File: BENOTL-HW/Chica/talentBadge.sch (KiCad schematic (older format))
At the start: 63 parts, among them P1 USB_A, P2 OLED, P3 Batt, P4 PS, P5 sd_card_spi, Q1 MMBT3904, Q2 MMBT3904, Q3 IR phototransistor, SW1 B1, SW2 B2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

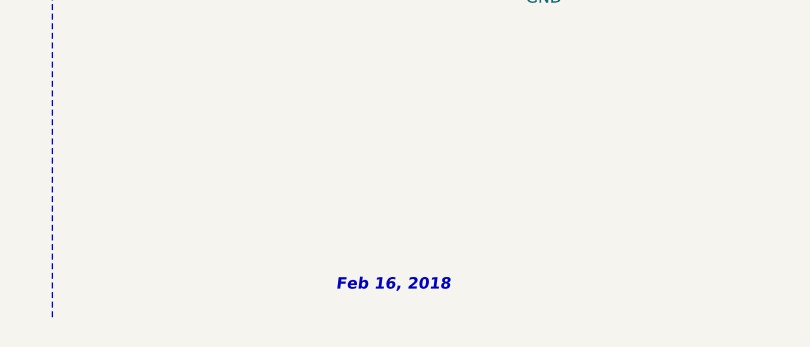
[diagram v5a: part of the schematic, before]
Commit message: Vinculado footprint ESP-WROOM-02
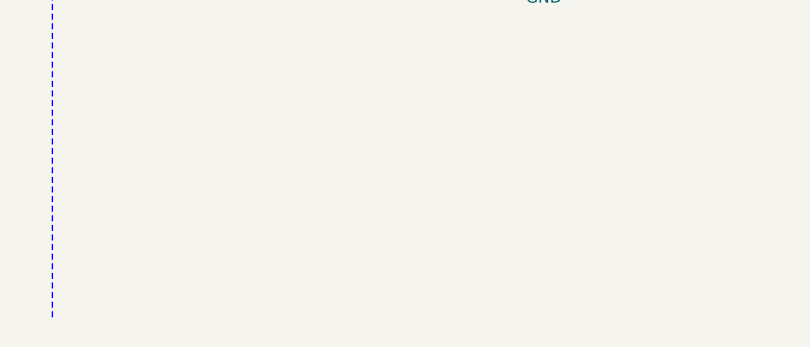
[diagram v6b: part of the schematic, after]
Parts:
- U1: footprint (none) -> talentBadge:ESP-13-WROOM-02
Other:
- note removed: "Feb 16, 2018\n"
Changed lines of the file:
@@
 $EndComp
 $Comp
-L GND #PWR8
+L GND #PWR01
 U 1 1 5A821F87
 P 2900 7450
-F 0 "#PWR8" H 2900 7200 50  0001 C CNN
+F 0 "#PWR01" H 2900 7200 50  0001 C CNN
 F 1 "GND" H 2900 7300 50  0000 C CNN
 F 2 "" H 2900 7450 50  0000 C CNN
@@
 $EndComp
 $Comp
-L GND #PWR6
+L GND #PWR02
 U 1 1 5A8731F6
 P 2550 3100
-F 0 "#PWR6" H 2550 2850 50  0001 C CNN
+F 0 "#PWR02" H 2550 2850 50  0001 C CNN
 F 1 "GND" H 2550 2950 50  0000 C CNN
 F 2 "" H 2550 3100 50  0000 C CNN
@@
 np1
 $Comp
-L GND #PWR11
+L GND #PWR03
 U 1 1 5A87C4F2
 P 4350 3100
-F 0 "#PWR11" H 4350 2850 50  0001 C CNN
+F 0 "#PWR03" H 4350 2850 50  0001 C CNN
 F 1 "GND" H 4350 2950 50  0000 C CNN
 F 2 "" H 4350 3100 50  0000 C CNN
@@
 np2
 $Comp
-L GND #PWR16
+L GND #PWR04
 U 1 1 5A87E79A
 P 6150 3100
-F 0 "#PWR16" H 6150 2850 50  0001 C CNN
+F 0 "#PWR04" H 6150 2850 50  0001 C CNN
 F 1 "GND" H 6150 2950 50  0000 C CNN
 F 2 "" H 6150 3100 50  0000 C CNN
@@
 $EndComp
 $Comp
-L GND #PWR3
+L GND #PWR05
 U 1 1 5A884E23
 P 1700 6900
-F 0 "#PWR3" H 1700 6650 50  0001 C CNN
+F 0 "#PWR05" H 1700 6650 50  0001 C CNN
 F 1 "GND" H 1700 6750 50  0000 C CNN
 F 2 "" H 1700 6900 50  0000 C CNN
@@
 $EndComp
 $Comp
-L +3.3V #PWR5
+L +3.3V #PWR06
 U 1 1 5A8855B6
 P 2250 6200
-F 0 "#PWR5" H 2250 6050 50  0001 C CNN
+F 0 "#PWR06" H 2250 6050 50  0001 C CNN
 F 1 "+3.3V" H 2250 6340 50  0000 C CNN
 F 2 "" H 2250 6200 50  0000 C CNN
@@
 np
 $Comp
-L +3.3V #PWR1
+L +3.3V #PWR07
 U 1 1 5A888CD9
 P 1000 950
-F 0 "#PWR1" H 1000 800 50  0001 C CNN
+F 0 "#PWR07" H 1000 800 50  0001 C CNN
 F 1 "+3.3V" H 1000 1090 50  0000 C CNN
 F 2 "" H 1000 950 50  0000 C CNN
@@
 $EndComp
 $Comp
-L +3.3V #PWR7
+L +3.3V #PWR08
 U 1 1 5A888D9D
 P 2850 950
-F 0 "#PWR7" H 2850 800 50  0001 C CNN
+F 0 "#PWR08" H 2850 800 50  0001 C CNN
 F 1 "+3.3V" H 2850 1090 50  0000 C CNN
 F 2 "" H 2850 950 50  0000 C CNN
@@
 $EndComp
 $Comp
-L +3.3V #PWR13
+L +3.3V #PWR09
 U 1 1 5A88959B
 P 4550 950
-F 0 "#PWR13" H 4550 800 50  0001 C CNN
+F 0 "#PWR09" H 4550 800 50  0001 C CNN
 F 1 "+3.3V" H 4550 1090 50  0000 C CNN
 F 2 "" H 4550 950 50  0000 C CNN
@@
 $EndComp
 $Comp
-L GND #PWR21
+L GND #PWR010
 U 1 1 5A889D35
 P 8100 2640
-F 0 "#PWR21" H 8100 2390 50  0001 C CNN
+F 0 "#PWR010" H 8100 2390 50  0001 C CNN
 F 1 "GND" H 8100 2490 50  0000 C CNN
 F 2 "" H 8100 2640 50  0000 C CNN
@@
 MISO
 $Comp
-L GND #PWR2
+L GND #PWR011
 U 1 1 5A89D556
 P 1400 4300
-F 0 "#PWR2" H 1400 4050 50  0001 C CNN
+F 0 "#PWR011" H 1400 4050 50  0001 C CNN
 F 1 "GND" H 1400 4150 50  0000 C CNN
 F 2 "" H 1400 4300 50  0000 C CNN
@@
 $EndComp
 $Comp
-L +3.3V #PWR4
+L +3.3V #PWR012
 U 1 1 5A89DD80
 P 1900 3850
-F 0 "#PWR4" H 1900 3700 50  0001 C CNN
+F 0 "#PWR012" H 1900 3700 50  0001 C CNN
 F 1 "+3.3V" H 1900 3990 50  0000 C CNN
 F 2 "" H 1900 3850 50  0000 C CNN
@@
 $EndComp
 $Comp
-L GND #PWR9
+L GND #PWR013
 U 1 1 5A8A120C
 P 3050 5200
-F 0 "#PWR9" H 3050 4950 50  0001 C CNN
+F 0 "#PWR013" H 3050 4950 50  0001 C CNN
 F 1 "GND" H 3050 5050 50  0000 C CNN
 F 2 "" H 3050 5200 50  0000 C CNN
@@
 	1    0    0    -1
 $EndComp
-Text Notes 8140 7640 0    50   Italic 10
-Feb 16, 2018\n
-$Comp
-L +3.3V #PWR23
+$Comp
+L +3.3V #PWR014
 U 1 1 5A8ACE92
 P 8750 4150
-F 0 "#PWR23" H 8750 4000 50  0001 C CNN
+F 0 "#PWR014" H 8750 4000 50  0001 C CNN
 F 1 "+3.3V" H 8750 4290 50  0000 C CNN
 F 2 "" H 8750 4150 50  0000 C CNN
@@
 $EndComp
 $Comp
-L GND #PWR22
+L GND #PWR015
 U 1 1 5A8B6B0C
 P 8600 4600
-F 0 "#PWR22" H 8600 4350 50  0001 C CNN
+F 0 "#PWR015" H 8600 4350 50  0001 C CNN
 F 1 "GND" H 8450 4550 50  0000 C CNN
 F 2 "" H 8600 4600 50  0000 C CNN
@@
 $EndComp
 $Comp
-L GND #PWR24
+L GND #PWR016
 U 1 1 5A8BA4F2
 P 9050 6200
-F 0 "#PWR24" H 9050 5950 50  0001 C CNN
+F 0 "#PWR016" H 9050 5950 50  0001 C CNN
 F 1 "GND" H 9050 6050 50  0000 C CNN
 F 2 "" H 9050 6200 50  0000 C CNN
@@
 $EndComp
 $Comp
-L +3.3V #PWR10
+L +3.3V #PWR017
 U 1 1 5A8CF103
 P 3700 6000
-F 0 "#PWR10" H 3700 5850 50  0001 C CNN
+F 0 "#PWR017" H 3700 5850 50  0001 C CNN
 F 1 "+3.3V" H 3700 6140 50  0000 C CNN
 F 2 "" H 3700 6000 50  0000 C CNN
@@
 $EndComp
 $Comp
-L +3.3V #PWR12
+L +3.3V #PWR018
 U 1 1 5A8CF265
 P 4535 4300
-F 0 "#PWR12" H 4535 4150 50  0001 C CNN
+F 0 "#PWR018" H 4535 4150 50  0001 C CNN
 F 1 "+3.3V" H 4535 4440 50  0000 C CNN
 F 2 "" H 4535 4300 50  0000 C CNN
@@
 $EndComp
 $Comp
-L GND #PWR14
+L GND #PWR019
 U 1 1 5A8CFC33
 P 4650 4900
-F 0 "#PWR14" H 4650 4650 50  0001 C CNN
+F 0 "#PWR019" H 4650 4650 50  0001 C CNN
 F 1 "GND" H 4650 4750 50  0000 C CNN
 F 2 "" H 4650 4900 50  0000 C CNN
@@
 IRL
 $Comp
-L GND #PWR18
+L GND #PWR020
 U 1 1 5A914774
 P 6200 5150
-F 0 "#PWR18" H 6200 4900 50  0001 C CNN
+F 0 "#PWR020" H 6200 4900 50  0001 C CNN
 F 1 "GND" H 6200 5000 50  0000 C CNN
 F 2 "" H 6200 5150 50  0000 C CNN
@@
 $EndComp
 $Comp
-L +3.3V #PWR17
+L +3.3V #PWR021
 U 1 1 5A916FB2
 P 6200 3850
-F 0 "#PWR17" H 6200 3700 50  0001 C CNN
+F 0 "#PWR021" H 6200 3700 50  0001 C CNN
 F 1 "+3.3V" H 6200 3990 50  0000 C CNN
 F 2 "" H 6200 3850 50  0000 C CNN
@@
 $EndComp
 $Comp
-L +3.3V #PWR19
+L +3.3V #PWR022
 U 1 1 5A8CED38
 P 7775 1585
-F 0 "#PWR19" H 7775 1435 50  0001 C CNN
+F 0 "#PWR022" H 7775 1435 50  0001 C CNN
 F 1 "+3.3V" H 7775 1725 50  0000 C CNN
 F 2 "" H 7775 1585 50  0000 C CNN
@@
 NoConn ~ 10550 4800
 $Comp
-L GND #PWR15
+L GND #PWR023
 U 1 1 5A9146B5
 P 5700 5150
-F 0 "#PWR15" H 5700 4900 50  0001 C CNN
+F 0 "#PWR023" H 5700 4900 50  0001 C CNN
 F 1 "GND" H 5700 5000 50  0000 C CNN
 F 2 "" H 5700 5150 50  0000 C CNN
@@
 F 0 "U1" H 9315 1940 50  0000 C CNN
 F 1 "ESP-13-WROOM-02" H 9315 2490 50  0000 C CNN
-F 2 "" H 9215 2040 50  0001 C CNN
+F 2 "talentBadge:ESP-13-WROOM-02" H 9215 2040 50  0001 C CNN
 F 3 "" H 9215 2040 50  0001 C CNN
 	1    9315 2040
@@
 Connection ~ 8030 1475
 $Comp
-L +3.3V #PWR20
+L +3.3V #PWR024
 U 1 1 5AA16781
 P 8025 1415
-F 0 "#PWR20" H 8025 1265 50  0001 C CNN
+F 0 "#PWR024" H 8025 1265 50  0001 C CNN
 F 1 "+3.3V" H 8025 1555 50  0000 C CNN
 F 2 "" H 8025 1415 50  0000 C CNN
@@
 $EndComp
 $Comp
-L GND #PWR25
+L GND #PWR025
 U 1 1 5AA16E5F
 P 10830 2575
-F 0 "#PWR25" H 10830 2325 50  0001 C CNN
+F 0 "#PWR025" H 10830 2325 50  0001 C CNN
 F 1 "GND" H 10830 2425 50  0000 C CNN
 F 2 "" H 10830 2575 50  0000 C CNN
@@
 	9315 2940 9315 3060
 $Comp
-L GND #PWR?
+L GND #PWR026
 U 1 1 5AA1CD61
 P 9315 3060
-F 0 "#PWR?" H 9315 2810 50  0001 C CNN
+F 0 "#PWR026" H 9315 2810 50  0001 C CNN
 F 1 "GND" H 9315 2910 50  0000 C CNN
 F 2 "" H 9315 3060 50  0000 C CNN

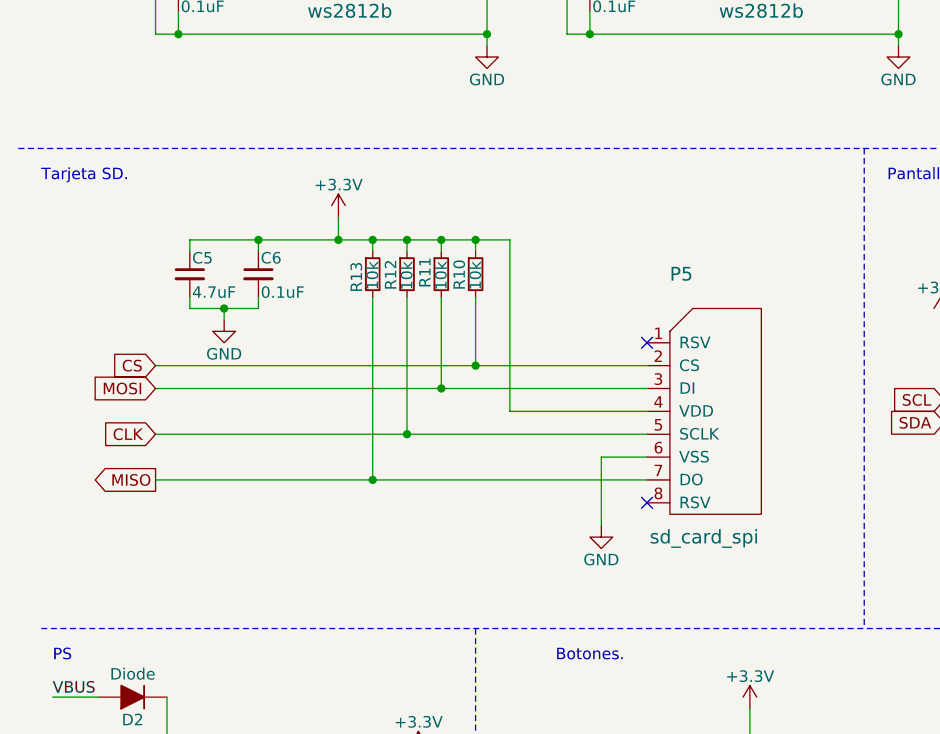
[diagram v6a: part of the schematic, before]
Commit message: Removido diagrama SD
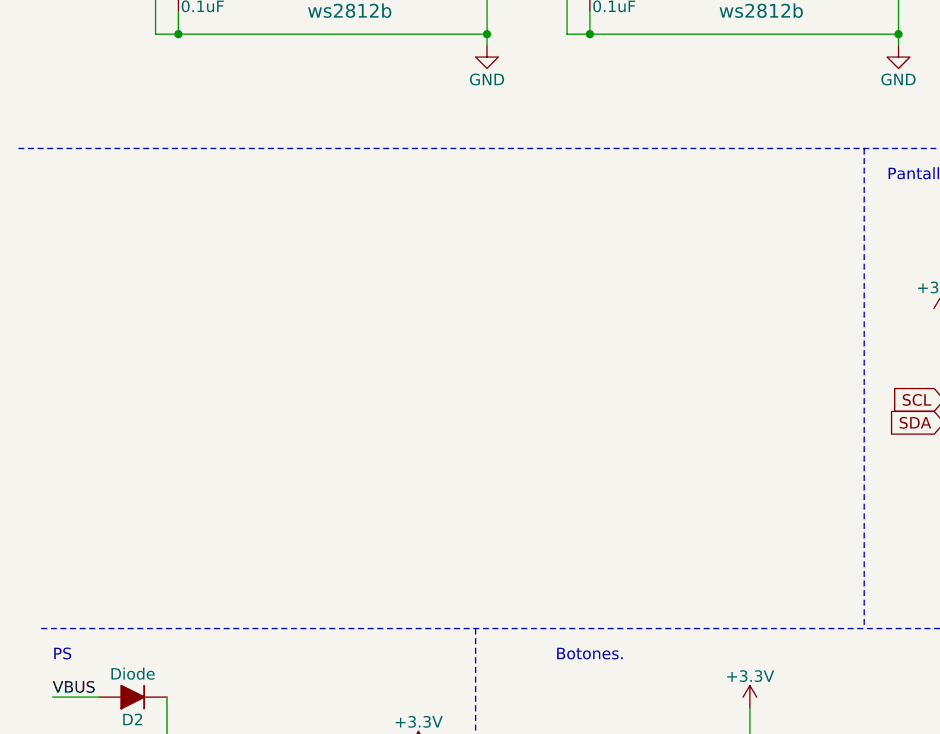
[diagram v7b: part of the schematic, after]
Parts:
- removed C5: 4.7uF, Capacitors_SMD:C_0805_HandSoldering, symbol C_Small
- removed C6: 0.1uF, Capacitors_SMD:C_0805_HandSoldering, symbol C_Small
- removed P5: sd_card_spi, talentBadge:MOLEX_0475710001, symbol sd_card_spi
- removed R10, R11, R12, R13: 10k, Resistors_SMD:R_0805_HandSoldering, symbol R_Small
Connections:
- no-connect marks 20 -> 18
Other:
- note removed: "Tarjeta SD."
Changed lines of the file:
@@
 Title "The badge of the Lands"
 Date "2018-03-07"
-Rev "0.3"
+Rev "0.4"
 Comp "Unofficial Badge of Talent Land 2018"
 Comment1 "Andres Sabas"
@@
 Text GLabel 10485 2535 2    50   Input ~ 0
 B2
-$Comp
-L sd_card_spi P5
-U 1 1 5A89AD86
-P 3550 5150
-F 0 "P5" H 3400 6200 60  0000 C CNN
-F 1 "sd_card_spi" H 3500 5050 60  0000 C CNN
-F 2 "talentBadge:MOLEX_0475710001" H 3550 5150 60  0001 C CNN
-F 3 "https://www.molex.com/pdm_docs/sd/475710001_sd.pdf" H 3550 5150 60  0001 C CNN
-F 4 "47571-0001 " H 3550 5150 60  0001 C CNN "PartNo"
-	1    3550 5150
-	1    0    0    -1
-$EndComp
-$Comp
-L R_Small R13
-U 1 1 5A89C226
-P 2050 4100
-F 0 "R13" V 1980 4020 50  0000 L CNN
-F 1 "10k" V 2050 4030 50  0000 L CNN
-F 2 "Resistors_SMD:R_0805_HandSoldering" H 2050 4100 50  0001 C CNN
-F 3 "https://www.mouser.com/ds/2/447/Yageo_08112016_RC0805-1211991.pdf" H 2050 4100 50  0001 C CNN
-F 4 "RC0805FR-0710KL" H 2050 4100 60  0001 C CNN "PartNo"
-	1    2050 4100
-	1    0    0    -1
-$EndComp
-$Comp
-L C_Small C5
-U 1 1 5A89C377
-P 1250 4100
-F 0 "C5" H 1260 4170 50  0000 L CNN
-F 1 "4.7uF" H 1260 4020 50  0000 L CNN
-F 2 "Capacitors_SMD:C_0805_HandSoldering" H 1250 4100 50  0001 C CNN
-F 3 "https://www.mouser.com/ds/2/40/TPS_AUTO-845414.pdf" H 1250 4100 50  0001 C CNN
-F 4 "TPSA475K010T1400 " H 1250 4100 60  0001 C CNN "PartNo"
-	1    1250 4100
-	1    0    0    -1
-$EndComp
-Text GLabel 1100 4500 0    50   Input ~ 0
-CS
-Text GLabel 1100 4600 0    50   Input ~ 0
-MOSI
-Text GLabel 1100 4800 0    50   Input ~ 0
-CLK
-Text GLabel 1100 5000 0    50   Output ~ 0
-MISO
-$Comp
-L GND #PWR011
-U 1 1 5A89D556
-P 1400 4300
-F 0 "#PWR011" H 1400 4050 50  0001 C CNN
-F 1 "GND" H 1400 4150 50  0000 C CNN
-F 2 "" H 1400 4300 50  0000 C CNN
-F 3 "" H 1400 4300 50  0000 C CNN
-	1    1400 4300
-	1    0    0    -1
-$EndComp
-$Comp
-L +3.3V #PWR012
-U 1 1 5A89DD80
-P 1900 3850
-F 0 "#PWR012" H 1900 3700 50  0001 C CNN
-F 1 "+3.3V" H 1900 3990 50  0000 C CNN
-F 2 "" H 1900 3850 50  0000 C CNN
-F 3 "" H 1900 3850 50  0000 C CNN
-	1    1900 3850
-	1    0    0    -1
-$EndComp
-$Comp
-L GND #PWR013
-U 1 1 5A8A120C
-P 3050 5200
-F 0 "#PWR013" H 3050 4950 50  0001 C CNN
-F 1 "GND" H 3050 5050 50  0000 C CNN
-F 2 "" H 3050 5200 50  0000 C CNN
-F 3 "" H 3050 5200 50  0000 C CNN
-	1    3050 5200
-	1    0    0    -1
-$EndComp
 $Comp
 L +3.3V #PWR014
@@
 Text Notes 4300 3700 0    50   ~ 0
 Pantalla OLED
-Text Notes 600  3700 0    50   ~ 0
-Tarjeta SD.
 Text Notes 650  5800 0    50   ~ 0
 PS
@@
 $EndComp
 $Comp
-L C_Small C6
-U 1 1 5A9285D5
-P 1550 4100
-F 0 "C6" H 1560 4170 50  0000 L CNN
-F 1 "0.1uF" H 1560 4020 50  0000 L CNN
-F 2 "Capacitors_SMD:C_0805_HandSoldering" H 1550 4100 50  0001 C CNN
-F 3 "https://www.mouser.com/ds/2/445/885012207045-554527.pdf" H 1550 4100 50  0001 C CNN
-F 4 "885012207045 " H 1550 4100 60  0001 C CNN "PartNo"
-	1    1550 4100
-	1    0    0    -1
-$EndComp
-$Comp
-L R_Small R12
-U 1 1 5A92A801
-P 2200 4100
-F 0 "R12" V 2130 4030 50  0000 L CNN
-F 1 "10k" V 2200 4030 50  0000 L CNN
-F 2 "Resistors_SMD:R_0805_HandSoldering" H 2200 4100 50  0001 C CNN
-F 3 "https://www.mouser.com/ds/2/447/Yageo_08112016_RC0805-1211991.pdf" H 2200 4100 50  0001 C CNN
-F 4 "RC0805FR-0710KL" H 2200 4100 60  0001 C CNN "PartNo"
-	1    2200 4100
-	1    0    0    -1
-$EndComp
-$Comp
-L R_Small R11
-U 1 1 5A92A8CD
-P 2350 4100
-F 0 "R11" V 2280 4040 50  0000 L CNN
-F 1 "10k" V 2350 4030 50  0000 L CNN
-F 2 "Resistors_SMD:R_0805_HandSoldering" H 2350 4100 50  0001 C CNN
-F 3 "https://www.mouser.com/ds/2/447/Yageo_08112016_RC0805-1211991.pdf" H 2350 4100 50  0001 C CNN
-F 4 "RC0805FR-0710KL" H 2350 4100 60  0001 C CNN "PartNo"
-	1    2350 4100
-	1    0    0    -1
-$EndComp
-$Comp
-L R_Small R10
-U 1 1 5A92A998
-P 2500 4100
-F 0 "R10" V 2430 4030 50  0000 L CNN
-F 1 "10k" V 2500 4030 50  0000 L CNN
-F 2 "Resistors_SMD:R_0805_HandSoldering" H 2500 4100 50  0001 C CNN
-F 3 "https://www.mouser.com/ds/2/447/Yageo_08112016_RC0805-1211991.pdf" H 2500 4100 50  0001 C CNN
-F 4 "RC0805FR-0710KL" H 2500 4100 60  0001 C CNN "PartNo"
-	1    2500 4100
-	1    0    0    -1
-$EndComp
-$Comp
 L R_Small R14
 U 1 1 5A92AC17
@@
 	1    0    0    -1
 $EndComp
-NoConn ~ 3250 5100
-NoConn ~ 3250 4400
 $Comp
 L CP2102N U2
@@
 Connection ~ 3700 6700
 Wire Wire Line
-	1100 5000 3250 5000
-Wire Wire Line
-	1100 4800 3250 4800
-Wire Wire Line
-	1100 4600 3250 4600
-Wire Wire Line
-	3250 4500 1100 4500
-Wire Wire Line
-	2500 4200 2500 4500
-Connection ~ 2500 4500
-Wire Wire Line
-	2350 4200 2350 4600
-Connection ~ 2350 4600
-Wire Wire Line
-	2200 4200 2200 4800
-Connection ~ 2200 4800
-Wire Wire Line
-	2050 4200 2050 5000
-Connection ~ 2050 5000
-Wire Wire Line
-	1250 4250 1550 4250
-Wire Wire Line
-	1550 4250 1550 4200
-Wire Wire Line
-	1250 4250 1250 4200
-Wire Wire Line
-	1400 4250 1400 4300
-Connection ~ 1400 4250
-Wire Wire Line
-	1250 4000 1250 3950
-Wire Wire Line
-	1250 3950 2650 3950
-Wire Wire Line
-	2500 3950 2500 4000
-Wire Wire Line
-	2350 4000 2350 3950
-Connection ~ 2350 3950
-Wire Wire Line
-	2200 4000 2200 3950
-Connection ~ 2200 3950
-Wire Wire Line
-	2050 4000 2050 3950
-Connection ~ 2050 3950
-Wire Wire Line
-	1550 4000 1550 3950
-Connection ~ 1550 3950
-Wire Wire Line
-	1900 3850 1900 3950
-Connection ~ 1900 3950
-Wire Wire Line
-	2650 3950 2650 4700
-Wire Wire Line
-	2650 4700 3250 4700
-Connection ~ 2500 3950
-Wire Wire Line
-	3050 5200 3050 4900
-Wire Wire Line
-	3050 4900 3250 4900
-Wire Wire Line
 	8750 4150 8750 4400

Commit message: Chica update
Actualizados caps C3 y C3
Cambio de silk antena
Cambio wroom.
Re routeo,
Cambio orientacion lcd
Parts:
- C3, C4: footprint Capacitors_SMD:C_0805_HandSoldering -> Capacitors_Tantalum_SMD:CP_Tantalum_Case-A_EIA-3216-18_Hand
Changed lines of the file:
@@
 LIBS:contrib
 LIBS:valves
-LIBS:ESP8266
+LIBS:pdxlbs
+LIBS:pspice
+LIBS:Video
+LIBS:Valve
+LIBS:Triac_Thyristor
+LIBS:Transistor_IGBT
+LIBS:Transistor_FET
+LIBS:Transistor_BJT
+LIBS:Transistor_Array
+LIBS:Transformer
+LIBS:Timer_RTC
+LIBS:Timer_PLL
+LIBS:Timer
+LIBS:Switch
+LIBS:Sensor_Voltage
+LIBS:Sensor_Touch
+LIBS:Sensor_Temperature
+LIBS:Sensor_Proximity
+LIBS:Sensor_Pressure
+LIBS:Sensor_Optical
+LIBS:Sensor_Motion
+LIBS:Sensor_Magnetic
+LIBS:Sensor_Humidity
+LIBS:Sensor_Gas
+LIBS:Sensor_Current
+LIBS:Sensor_Audio
+LIBS:Sensor
+LIBS:Relay_SolidState
+LIBS:Relay
+LIBS:Regulator_Switching
+LIBS:Regulator_SwitchedCapacitor
+LIBS:Regulator_Linear
+LIBS:Regulator_Current
+LIBS:Regulator_Controller
+LIBS:Reference_Voltage
+LIBS:Reference_Current
+LIBS:RF_ZigBee
+LIBS:RF_WiFi
+LIBS:RF_Switch
+LIBS:RF_RFID
+LIBS:RF_Module
+LIBS:RF_Mixer
+LIBS:RF_GPS
+LIBS:RF_Bluetooth
+LIBS:RF_AM_FM
+LIBS:RF
+LIBS:Power_Supervisor
+LIBS:Power_Protection
+LIBS:Power_Management
+LIBS:Potentiometer_Digital
+LIBS:Oscillator
+LIBS:Motor
+LIBS:Memory_UniqueID
+LIBS:Memory_ROM
+LIBS:Memory_RAM
+LIBS:Memory_NVRAM
+LIBS:Memory_Flash
+LIBS:Memory_EPROM
+LIBS:Memory_EEPROM
+LIBS:Memory_Controller
+LIBS:Mechanical
+LIBS:MCU_Texas_MSP430
+LIBS:MCU_Texas
+LIBS:MCU_SiliconLabs
+LIBS:MCU_SiFive
+LIBS:MCU_ST_STM8
+LIBS:MCU_ST_STM32
+LIBS:MCU_Parallax
+LIBS:MCU_NXP_S08
+LIBS:MCU_NXP_MCore
+LIBS:MCU_NXP_MAC7100
+LIBS:MCU_NXP_LPC
+LIBS:MCU_NXP_Kinetis
+LIBS:MCU_NXP_HCS12
+LIBS:MCU_NXP_HC12
+LIBS:MCU_NXP_HC11
+LIBS:MCU_NXP_ColdFire
+LIBS:MCU_Module
+LIBS:MCU_Microchip_SAML
+LIBS:MCU_Microchip_SAME
+LIBS:MCU_Microchip_PIC32
+LIBS:MCU_Microchip_PIC24
+LIBS:MCU_Microchip_PIC18
+LIBS:MCU_Microchip_PIC16
+LIBS:MCU_Microchip_PIC12
+LIBS:MCU_Microchip_PIC10
+LIBS:MCU_Intel
+LIBS:MCU_Infineon
+LIBS:MCU_Cypress
+LIBS:MCU_Atmel_AVR
+LIBS:MCU_Atmel_ATTINY
+LIBS:MCU_Atmel_ATMEGA
+LIBS:MCU_Atmel_8051
+LIBS:MCU_AnalogDevices
+LIBS:Logic_TTL_IEEE
+LIBS:Logic_Programmable
+LIBS:Logic_LevelTranslator
+LIBS:Logic_CMOS_IEEE
+LIBS:Logic_CMOS_4000
+LIBS:Logic_74xx
+LIBS:Logic_74xgxx
+LIBS:LED
+LIBS:Jumper
+LIBS:Isolator_Analog
+LIBS:Isolator
+LIBS:Interface_USB
+LIBS:Interface_UART
+LIBS:Interface_Telecom
+LIBS:Interface_Optical
+LIBS:Interface_LineDriver
+LIBS:Interface_HID
+LIBS:Interface_Expansion
+LIBS:Interface_Ethernet
+LIBS:Interface_CurrentLoop
+LIBS:Interface_CAN_LIN
+LIBS:Interface
+LIBS:Graphic
+LIBS:GPU
+LIBS:Filter
+LIBS:FPGA_Xilinx_Virtex7
+LIBS:FPGA_Xilinx_Virtex6
+LIBS:FPGA_Xilinx_Virtex5
+LIBS:FPGA_Xilinx_Spartan6
+LIBS:FPGA_Xilinx_Kintex7
+LIBS:FPGA_Xilinx_Artix7
+LIBS:FPGA_Xilinx
+LIBS:FPGA_Actel
+LIBS:Driver_Relay
+LIBS:Driver_Motor
+LIBS:Driver_LED
+LIBS:Driver_FET
+LIBS:Driver_Display
+LIBS:Display_Graphic
+LIBS:Display_Character
+LIBS:Diode_Laser
+LIBS:Diode_Bridge
+LIBS:Diode
+LIBS:Device
+LIBS:DSP_Texas
+LIBS:DSP_Motorola
+LIBS:DSP_Microchip_DSPIC33
+LIBS:DSP_Freescale
+LIBS:Converter_DCDC
+LIBS:Converter_ACDC
+LIBS:Connector_Specialized
+LIBS:Connector_Generic_Shielded
+LIBS:Connector_Generic
+LIBS:Comparator
+LIBS:CPU_PowerPC
+LIBS:CPU_NXP_68000
+LIBS:CPU_NXP_6800
+LIBS:CPU
+LIBS:CPLD_Xilinx
+LIBS:CPLD_Altera
+LIBS:Battery_Management
+LIBS:Audio
+LIBS:Analog_Switch
+LIBS:Analog_DAC
+LIBS:Analog_ADC
+LIBS:Analog
+LIBS:Amplifier_Video
+LIBS:Amplifier_Operational
+LIBS:Amplifier_Instrumentation
+LIBS:Amplifier_Difference
+LIBS:Amplifier_Current
+LIBS:Amplifier_Buffer
+LIBS:Amplifier_Audio
 LIBS:talentBadge-cache
 EELAYER 25 0
@@
 F 0 "C3" H 1160 6670 50  0000 L CNN
 F 1 "4.7uF" H 1160 6520 50  0000 L CNN
-F 2 "Capacitors_SMD:C_0805_HandSoldering" H 1150 6600 50  0001 C CNN
+F 2 "Capacitors_Tantalum_SMD:CP_Tantalum_Case-A_EIA-3216-18_Hand" H 1150 6600 50  0001 C CNN
 F 3 "https://www.mouser.com/ds/2/40/TPS_AUTO-845414.pdf" H 1150 6600 50  0001 C CNN
 F 4 "TPSA475K010T1400" H 1150 6600 60  0001 C CNN "PartNo"
@@
 F 0 "C4" H 2260 6670 50  0000 L CNN
 F 1 "4.7uF" H 2260 6520 50  0000 L CNN
-F 2 "Capacitors_SMD:C_0805_HandSoldering" H 2250 6600 50  0001 C CNN
+F 2 "Capacitors_Tantalum_SMD:CP_Tantalum_Case-A_EIA-3216-18_Hand" H 2250 6600 50  0001 C CNN
 F 3 "https://www.mouser.com/ds/2/40/TPS_AUTO-845414.pdf" H 2250 6600 50  0001 C CNN
 F 4 "TPSA475K010T1400" H 2250 6600 60  0001 C CNN "PartNo"
